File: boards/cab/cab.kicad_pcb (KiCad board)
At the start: 4 copper layers, 71.3 x 71.3 mm, 45 parts, among them J1 Conn_01x08_Female, J2 Conn_01x08_Female, J3 Conn_01x08_Female, J4 Conn_01x08_Female, Q1 SI2308A, Q2 S8550, Q3 BC817-40,215, Q4 S8550, Q5 BC817-40,215, Q6 S8550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

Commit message: PCB
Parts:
- J1, J2, J3, J4: moved to B.Cu
- turned J1 to 90 degrees
- turned J2 to 0 degrees
- turned J3 to -90 degrees
- turned J4 to 180 degrees

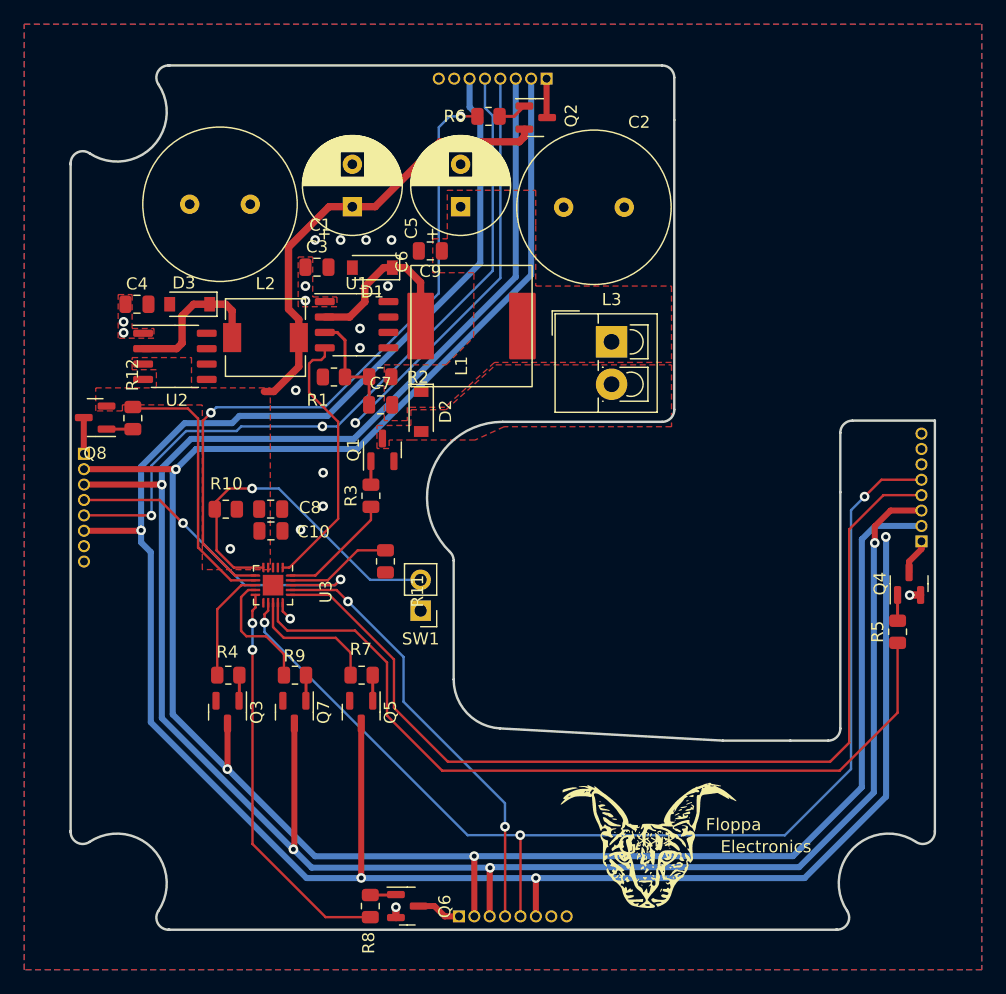
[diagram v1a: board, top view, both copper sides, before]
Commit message: Added LED resistors, changed routing
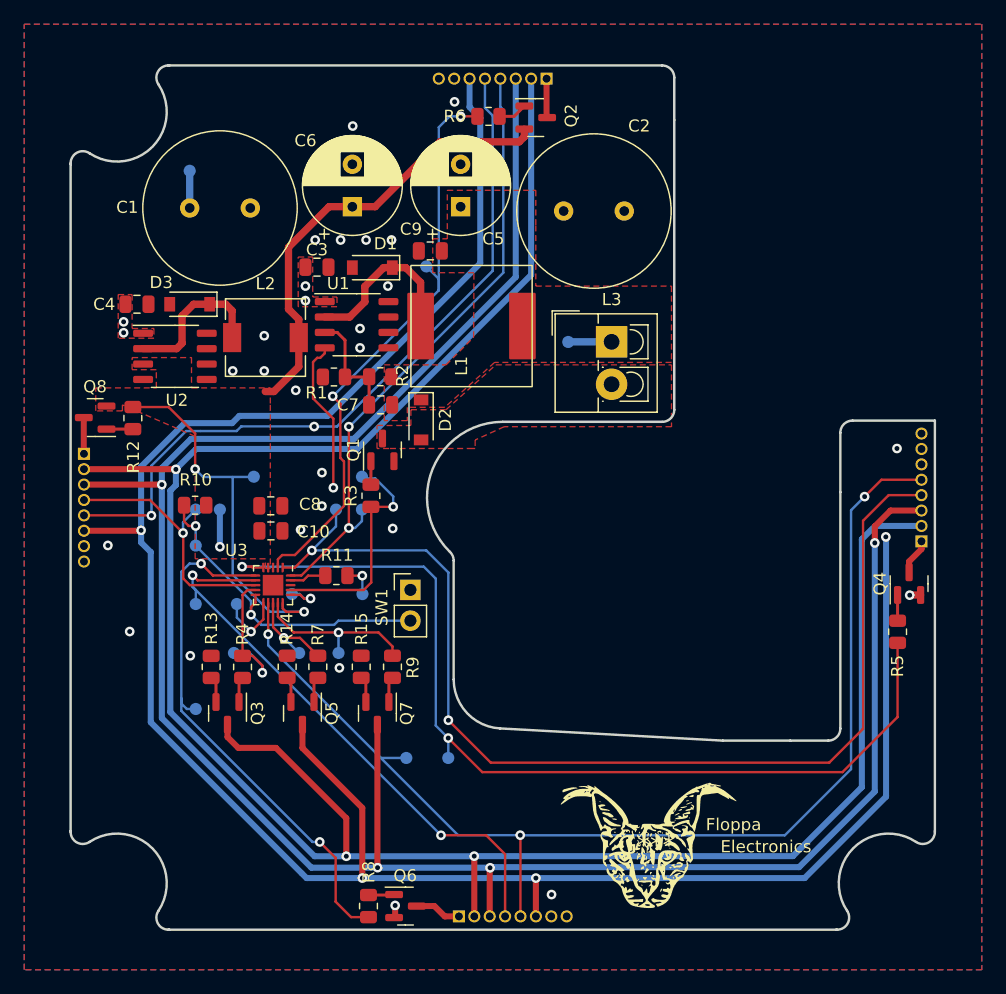
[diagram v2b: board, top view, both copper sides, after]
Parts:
- added R13: 1k, Resistor_SMD:R_0805_2012Metric, F.Cu at (70.4, 93.0)
- added R14: 1k, Resistor_SMD:R_0805_2012Metric, F.Cu at (76.7, 93.0)
- added R15: 1k, Resistor_SMD:R_0805_2012Metric, F.Cu at (82.8, 93.0)
- added TP1: UPDI, StackCabinet:testpad, F.Cu at (82.9, 87.0)
- added TP10: SEL0, StackCabinet:testpad, F.Cu at (82.9, 80.0)
- added TP11: SEL1, StackCabinet:testpad, F.Cu at (80.7, 80.0)
- added TP12: SEL2, StackCabinet:testpad, F.Cu at (69.2, 87.8)
- added TP13: SEL3, StackCabinet:testpad, F.Cu at (69.2, 80.0)
- added TP14: R_PWM, StackCabinet:testpad, F.Cu at (72.3, 91.9)
- added TP15: G_PWM, StackCabinet:testpad, F.Cu at (77.7, 91.9)
- added TP16: B_PWM, StackCabinet:testpad, F.Cu at (80.9, 91.9)
- added TP17: LED0_PWM, StackCabinet:testpad, F.Cu at (88.2, 60.0)
- added TP18: LED1_PWM, StackCabinet:testpad, F.Cu at (90.0, 100.5)
- added TP19: LED2_PWM, StackCabinet:testpad, F.Cu at (69.2, 96.5)
- added TP2: RxD, StackCabinet:testpad, F.Cu at (72.5, 87.8)
- added TP20: LED3_PWM, StackCabinet:testpad, F.Cu at (73.9, 77.3)
- added TP3: GDA, StackCabinet:testpad, F.Cu at (86.5, 100.5)
- added TP4: VBUS, StackCabinet:testpad, F.Cu at (68.7, 52.1)
- added TP5: 5V, StackCabinet:testpad, F.Cu at (71.1, 80.0)
- added TP6: 24V, StackCabinet:testpad, F.Cu at (99.9, 66.2)
- added TP7: CAB_STATE, StackCabinet:testpad, F.Cu at (69.2, 83.0)
- added TP8: 24V_EN, StackCabinet:testpad, F.Cu at (77.1, 87.0)
- added TP9: SOL_EN, StackCabinet:testpad, F.Cu at (82.9, 77.3)
- moved R9 8.07 mm to (85.4, 93.0), turned to -90 degrees
- moved Q7 6.85 mm to (84.1, 96.8)
- moved Q5 4.85 mm to (78.0, 96.8)
- moved R11 4.22 mm to (80.8, 85.5), turned to 0 degrees
- moved R7 3.68 mm to (79.2, 93.0), turned to -90 degrees
- moved R10 2.55 mm to (69.1, 79.7)
- moved SW1 1.91 mm to (86.9, 86.7), turned to 0 degrees
- moved R4 1.36 mm to (73.0, 93.0), turned to -90 degrees
- moved D2 0.69 mm to (87.7, 72.6)
- moved C1 0.31 mm to (68.7, 55.2)
- moved C2 0.31 mm to (104.5, 55.4)
- moved C8 0.27 mm to (75.3, 79.7)
- moved Q6 0.15 mm to (86.5, 112.8)
- moved R8 0.15 mm to (83.4, 112.8)
- moved Q3 0.10 mm to (71.8, 96.8)
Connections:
- Q3 pad 2: GND -> Net-(Q3-Pad2)
- Q5 pad 2: GND -> Net-(Q5-Pad2)
- Q7 pad 2: GND -> Net-(Q7-Pad2)
- U1 pad 6: GND -> (no net)
- U1 pad 7: GND -> (no net)
- U1 pad 8: GND -> (no net)
- U2 pad 6: GND -> (no net)
- U2 pad 7: GND -> (no net)
- U2 pad 8: GND -> (no net)
- U3 pad 1: 24V_EN -> SEL1
- U3 pad 10: LED2_PWM -> CAB_STATE
- U3 pad 14: LED1_PWM -> B_PWM
- U3 pad 15: SEL0 -> LED3_PWM
- U3 pad 16: SEL1 -> 24V_EN
- U3 pad 17: SEL2 -> SOL_EN
- U3 pad 18: SEL3 -> unconnected-(U3-Pad18)
- U3 pad 2: unconnected-(U3-Pad2) -> LED0_PWM
- U3 pad 20: SOL_EN -> SEL0
- U3 pad 5: CAB_STATE -> LED1_PWM
- U3 pad 6: LED0_PWM -> LED2_PWM
- U3 pad 7: LED3_PWM -> SEL2
- U3 pad 8: R_PWM -> SEL3
- U3 pad 9: B_PWM -> R_PWM
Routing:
- net R: track 178.7 -> 191.8 mm
- net LED2_PWM: track 32.9 -> 44.8 mm
- net SEL1: track 79.5 -> 91.1 mm, vias 0 -> 2
- net LED1_PWM: track 68.1 -> 79.6 mm, vias 0 -> 2
- net SEL2: track 36.5 -> 47.9 mm
- net SOL_EN: track 9.61 -> 19.1 mm, vias 0 -> 1
- net LED3_PWM: track 22.3 -> 31.7 mm, vias 0 -> 2
- net LED0_PWM: track 56.6 -> 49.2 mm
- net SEL3: track 28.6 -> 21.6 mm, vias 2 -> 1
- net Net-(R11-Pad1): track 8.85 -> 3.02 mm
- net RxD: track 0.00 -> 5.57 mm, vias 0 -> 1
- net 24V_EN: track 22.3 -> 26.2 mm, vias 0 -> 2
- net B_PWM: track 10.3 -> 13.9 mm, vias 0 -> 1
- net 24V: track 0.00 -> 3.58 mm
- net 5V: track 132.6 -> 136.2 mm
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
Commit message: Added silklayer text and generated gerber
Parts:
- U1, U2: footprint Package_SO:SOP-8_3.9x4.9mm_P1.27mm -> StackCabinet:XLE1509
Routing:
- net GND: vias 23 -> 28
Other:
- board text added: "11/2022"
- board text added: "B"
- board text added: "Bart Vonk"
- board text added: "G"
- board text added: "GDA"
- board text added: "GND"
- board text added: "In collaboration with Stakt"
- board text added: "JLCJLCJLCJLC"
- board text added: "LED0"
- board text added: "LED1"
- board text added: "LED2"
- board text added: "LED3"
- board text added: "R"
- board text added: "SEL0"
- board text added: "SEL1"
- board text added: "SEL2"
- board text added: "SEL3"
- board text added: "Stefan de Kraker"
- board text added: "VBUS"
